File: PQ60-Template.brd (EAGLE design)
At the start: 44 x 44 mm, 3 parts, among them X1-BOT FX8C-60S-SV, X1-TOP FX8C-60P-SV

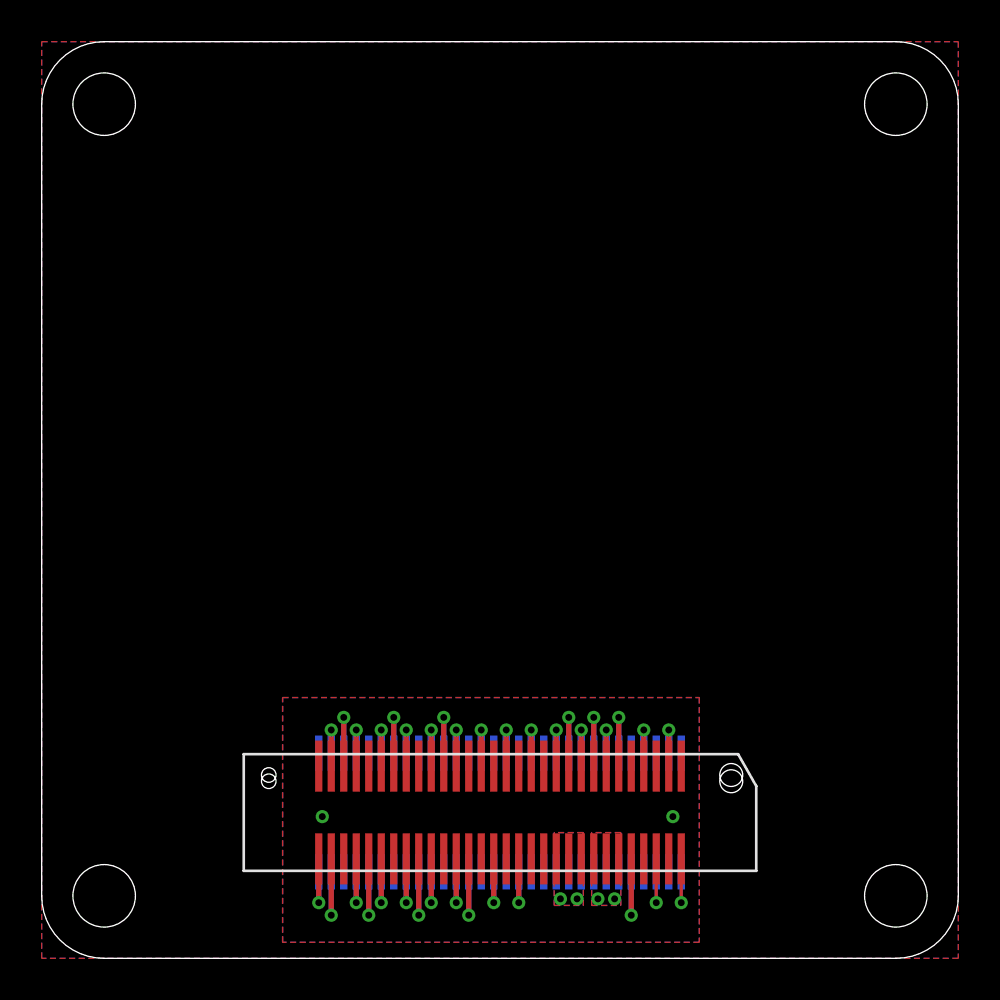
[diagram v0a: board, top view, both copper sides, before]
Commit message: Update to new PQ60 v1.1 standard.
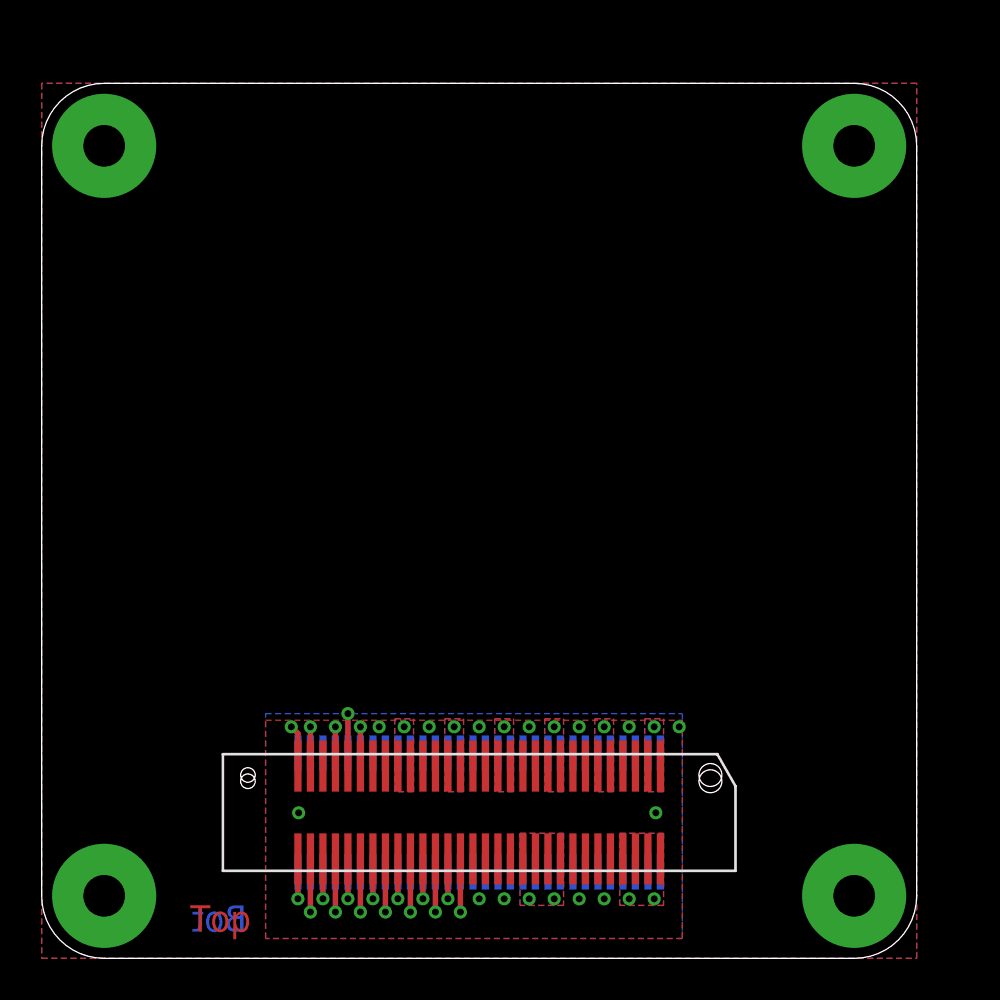
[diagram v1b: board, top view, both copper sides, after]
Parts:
- B1: value PQ60-NOPINS -> PQ60-PINS; device general:PQ60_NOPINS -> general:PQ60_PINS
- moved X1-BOT 1.00 mm to (21.0, 7.00)
- moved X1-TOP 1.00 mm to (21.0, 7.00)
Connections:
- removed net +3V3: X1-BOT.50, X1-BOT.51, X1-BOT.52, X1-TOP.50, X1-TOP.51, X1-TOP.52
- removed net GPIO[13]: X1-BOT.39, X1-TOP.39
- removed net GPIO[14]: X1-BOT.40, X1-TOP.40
- removed net NC@34: X1-BOT.34, X1-TOP.34
- removed net NC@35: X1-BOT.35, X1-TOP.35
- removed net NC@36: X1-BOT.36, X1-TOP.36
- removed net NC@42: X1-BOT.42, X1-TOP.42
- removed net NC@43: X1-BOT.43, X1-TOP.43
- removed net NC@56: X1-BOT.56, X1-TOP.56
- removed net SPI_CS: X1-BOT.47, X1-TOP.47
- removed net USB_N: X1-BOT.58, X1-TOP.58
- removed net USB_P: X1-BOT.60, X1-TOP.60
- removed net VBUS: X1-BOT.53, X1-BOT.54, X1-BOT.55, X1-TOP.53, X1-TOP.54, X1-TOP.55
- removed net VBUS_SW[1]: X1-BOT.6, X1-TOP.6
- removed net VBUS_SW[2]: X1-BOT.7, X1-TOP.7
- removed net VBUS_SW[3]: X1-BOT.8, X1-TOP.8
- new net GPIO[0]: X1-BOT.25, X1-TOP.25
- new net PRO1: X1-BOT.57, X1-BOT.58, X1-BOT.59, X1-BOT.60, X1-TOP.57, X1-TOP.58, X1-TOP.59, X1-TOP.60
- new net VBAT: X1-BOT.49, X1-BOT.50, X1-BOT.51, X1-BOT.52, X1-TOP.49, X1-TOP.50, X1-TOP.51, X1-TOP.52
- new net VBAT_SW[1]: X1-BOT.13, X1-BOT.14, X1-TOP.13, X1-TOP.14
- new net VBAT_SW[2]: X1-BOT.17, X1-BOT.18, X1-TOP.17, X1-TOP.18
- new net VBAT_SW[3]: X1-BOT.21, X1-BOT.22, X1-TOP.21, X1-TOP.22
- net !RST: now also X1-BOT.27, X1-TOP.27; no longer X1-BOT.45, X1-TOP.45
- net +3V3_SW[1]: now also X1-BOT.1, X1-BOT.2, X1-TOP.1, X1-TOP.2; no longer X1-BOT.9, X1-TOP.9
- net +3V3_SW[2]: now also X1-BOT.5, X1-BOT.6, X1-TOP.5, X1-TOP.6; no longer X1-BOT.10, X1-TOP.10
- net +3V3_SW[3]: now also X1-BOT.10, X1-BOT.9, X1-TOP.10, X1-TOP.9; no longer X1-BOT.11, X1-TOP.11
- net GND: now also X1-BOT.11, X1-BOT.15, X1-BOT.19, X1-BOT.20, X1-BOT.23, X1-BOT.24, X1-BOT.28, X1-BOT.4, X1-BOT.45, X1-BOT.47, X1-BOT.53, X1-BOT.54, X1-BOT.55, X1-BOT.56, X1-BOT.7, X1-BOT.8, X1-TOP.11, X1-TOP.15, X1-TOP.19, X1-TOP.20, X1-TOP.23, X1-TOP.24, X1-TOP.28, X1-TOP.4, X1-TOP.45, X1-TOP.47, X1-TOP.53, X1-TOP.54, X1-TOP.55, X1-TOP.56, X1-TOP.7, X1-TOP.8; no longer X1-BOT.1, X1-BOT.14, X1-BOT.18, X1-BOT.22, X1-BOT.26, X1-BOT.30, X1-BOT.33, X1-BOT.37, X1-BOT.41, X1-BOT.44, X1-BOT.49, X1-BOT.5, X1-BOT.57, X1-BOT.59, X1-TOP.1, X1-TOP.14, X1-TOP.18, X1-TOP.22, X1-TOP.26, X1-TOP.30, X1-TOP.33, X1-TOP.37, X1-TOP.41, X1-TOP.44, X1-TOP.49, X1-TOP.5, X1-TOP.57, X1-TOP.59
- net GPIO[10]: now also X1-BOT.42, X1-TOP.42; no longer X1-BOT.31, X1-TOP.31
- net GPIO[11]: now also X1-BOT.43, X1-TOP.43; no longer X1-BOT.32, X1-TOP.32
- net GPIO[12]: now also X1-BOT.44, X1-TOP.44; no longer X1-BOT.38, X1-TOP.38
- net GPIO[1]: now also X1-BOT.26, X1-TOP.26; no longer X1-BOT.19, X1-TOP.19
- net GPIO[2]: now also X1-BOT.34, X1-TOP.34; no longer X1-BOT.20, X1-TOP.20
- net GPIO[3]: now also X1-BOT.35, X1-TOP.35; no longer X1-BOT.21, X1-TOP.21
- net GPIO[4]: now also X1-BOT.36, X1-TOP.36; no longer X1-BOT.23, X1-TOP.23
- net GPIO[5]: now also X1-BOT.37, X1-TOP.37; no longer X1-BOT.24, X1-TOP.24
- net GPIO[6]: now also X1-BOT.38, X1-TOP.38; no longer X1-BOT.25, X1-TOP.25
- net GPIO[7]: now also X1-BOT.39, X1-TOP.39; no longer X1-BOT.27, X1-TOP.27
- net GPIO[8]: now also X1-BOT.40, X1-TOP.40; no longer X1-BOT.28, X1-TOP.28
- net GPIO[9]: now also X1-BOT.41, X1-TOP.41; no longer X1-BOT.29, X1-TOP.29
- net I2C_SCL: now also X1-BOT.29, X1-TOP.29; no longer X1-BOT.2, X1-TOP.2
- net I2C_SDA: now also X1-BOT.30, X1-TOP.30; no longer X1-BOT.4, X1-TOP.4
- net SPI_MISO: now also X1-BOT.32, X1-TOP.32; no longer X1-BOT.15, X1-TOP.15
- net SPI_MOSI: now also X1-BOT.31, X1-TOP.31; no longer X1-BOT.17, X1-TOP.17
- net SPI_SCK: now also X1-BOT.33, X1-TOP.33; no longer X1-BOT.13, X1-TOP.13
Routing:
- net NC@56: track 4.79 -> 0.00 mm, vias 1 -> 0
- net NC@43: track 4.79 -> 0.00 mm, vias 1 -> 0
- net NC@35: track 4.79 -> 0.00 mm, vias 1 -> 0
- net GPIO[13]: track 4.79 -> 0.00 mm, vias 1 -> 0
- net VBUS_SW[3]: track 4.05 -> 0.00 mm, vias 1 -> 0
- net VBUS_SW[1]: track 4.05 -> 0.00 mm, vias 1 -> 0
- net +3V3_SW[2]: track 4.05 -> 0.00 mm
- net USB_P: track 3.58 -> 0.00 mm, vias 1 -> 0
- net USB_N: track 3.58 -> 0.00 mm, vias 1 -> 0
- net SPI_CS: track 3.58 -> 0.00 mm, vias 1 -> 0
- net NC@42: track 3.58 -> 0.00 mm, vias 1 -> 0
- net NC@36: track 3.58 -> 0.00 mm, vias 1 -> 0
- net NC@34: track 3.58 -> 0.00 mm, vias 1 -> 0
- net GPIO[14]: track 3.58 -> 0.00 mm, vias 1 -> 0
- net GPIO[0]: track 0.00 -> 3.15 mm, vias 0 -> 1
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- added copper zone on layer 1, net +3V3_SW[1]
- added copper zone on layer 16, net +3V3_SW[1]
- added copper zone on layer 1, net +3V3_SW[2]
- added copper zone on layer 16, net +3V3_SW[2]
- added copper zone on layer 1, net +3V3_SW[3]
- added copper zone on layer 16, net +3V3_SW[3]
- added copper zone on layer 1, net PRO1
- added copper zone on layer 16, net PRO1
- added copper zone on layer 1, net VBAT
- added copper zone on layer 16, net VBAT
- added copper zone on layer 1, net VBAT_SW[1]
- added copper zone on layer 16, net VBAT_SW[1]
- added copper zone on layer 1, net VBAT_SW[2]
- added copper zone on layer 16, net VBAT_SW[2]
- added copper zone on layer 1, net VBAT_SW[3]
- added copper zone on layer 16, net VBAT_SW[3]
- removed copper zone on layer 1, net +3V3
- removed copper zone on layer 16, net +3V3
- removed copper zone on layer 1, net VBUS
- removed copper zone on layer 16, net VBUS
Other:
- board size 44 x 44 mm -> 42 x 42 mm
- board text added: "Bot"
- board text added: "Top"
